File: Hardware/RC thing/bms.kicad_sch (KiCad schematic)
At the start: 6 parts, among them U1 MCP73831-2-OT

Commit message: 90%
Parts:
- added C401: 10u, Capacitor_SMD:C_0805_2012Metric_Pad1.18x1.45mm_HandSolder, symbol Device:C
- added C404: 22u, Capacitor_SMD:C_0805_2012Metric_Pad1.18x1.45mm_HandSolder, symbol Device:C
- added L402: 2.2u, Inductor_SMD:L_APV_ANR252012, symbol Device:L
- added R403: 100k, Resistor_SMD:R_0603_1608Metric_Pad0.98x0.95mm_HandSolder, symbol Device:R
- added R404: 160k, Resistor_SMD:R_0603_1608Metric_Pad0.98x0.95mm_HandSolder, symbol Device:R
- added R405: 51k, Resistor_SMD:R_0603_1608Metric_Pad0.98x0.95mm_HandSolder, symbol Device:R
- added U401: TPS62170DSG, Package_SON:WSON-8-1EP_2x2mm_P0.5mm_EP0.9x1.6mm_ThermalVias, symbol Regulator_Switching:TPS62170DSG
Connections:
- net +3.3V: now also C404.1, L402.2, R403.2, R404.2, U401.6 (VOS)
- net GND: now also C401.2, C404.2, R403.1, R405.1, U401.1 (PGND), U401.4 (AGND), U401.8 (PG), U401.9 (PAD)
- net VBAT: now also C401.1, U401.2 (VIN), U401.3 (EN)
- net VDC renamed VUSB
- new net: R404.1, R405.2, U401.5 (FB)
- new net: L402.1, U401.7 (SW)
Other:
- note added: "Buck converter - 3.3V"

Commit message: more rc stuff (trust)
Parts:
- removed R1: R, symbol Device:R
- added C409: 100n, Capacitor_SMD:C_0603_1608Metric_Pad1.08x0.95mm_HandSolder, symbol Device:C
- added R410: 200k, Resistor_SMD:R_0603_1608Metric_Pad0.98x0.95mm_HandSolder, symbol Device:R
- added R411: 130k, Resistor_SMD:R_0603_1608Metric_Pad0.98x0.95mm_HandSolder, symbol Device:R
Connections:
- net GND: now also C409.2, R411.2
- net VBAT: now also R410.1
- net Batt_status renamed Charge_status
- new net Battery_voltage_level: C409.1, R410.2, R411.1
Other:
- note added: "BMS/Charging IC"
- note added: "Battery voltage level"
- moved on the sheet: BT1, C1, C2, C401, C404, L402, R2, R403, R404, R405, U1, U401

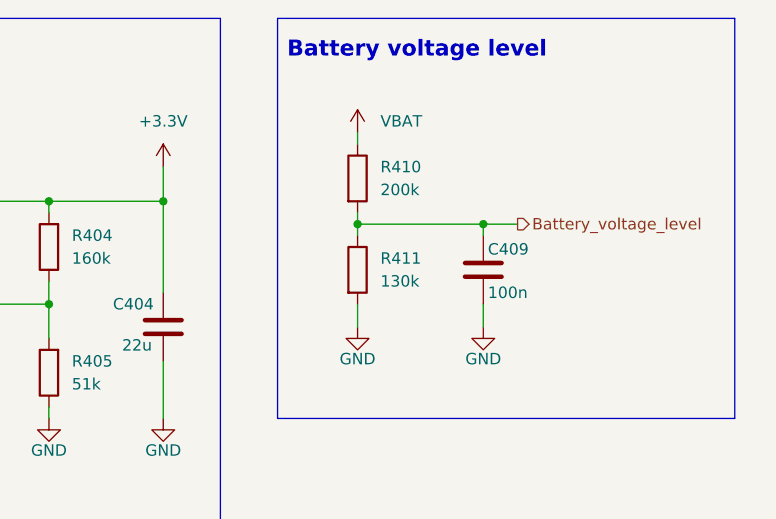
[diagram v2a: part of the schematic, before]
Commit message: fixed voltage divider for controller batt status
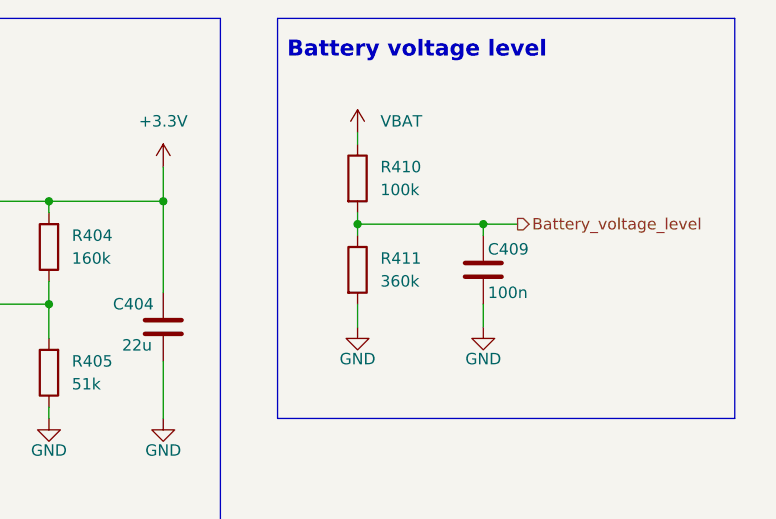
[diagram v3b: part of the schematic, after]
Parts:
- R410: value 200k -> 100k
- R411: value 130k -> 360k
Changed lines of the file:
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@@
 			)
 		)
-		(property "Value" "130k"
+		(property "Value" "360k"
 			(at 227.33 48.2599 0)
 			(effects
@@
 			)
 		)
-		(property "Value" "200k"
+		(property "Value" "100k"
 			(at 227.33 38.0999 0)
 			(effects

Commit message: RC thing PCB 95% trustworthy (six seven)
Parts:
- added D2: LED, Diode_SMD:D_0603_1608Metric_Pad1.05x0.95mm_HandSolder, symbol Device:LED
- added R1: 240, Resistor_SMD:R_0603_1608Metric_Pad0.98x0.95mm_HandSolder, symbol Device:R
- added SW1: Bat_switch, Connector_JST:JST_PH_B2B-PH-K_1x02_P2.00mm_Vertical, symbol Switch:SW_SPST
- BT1: footprint (none) -> Connector_JST:JST_PH_B2B-PH-K_1x02_P2.00mm_Vertical
- C18: renamed from C2; footprint (none) -> Capacitor_SMD:C_0805_2012Metric_Pad1.18x1.45mm_HandSolder
- C20: renamed from C1; footprint (none) -> Capacitor_SMD:C_0805_2012Metric_Pad1.18x1.45mm_HandSolder
- R2: footprint (none) -> Resistor_SMD:R_0603_1608Metric_Pad0.98x0.95mm_HandSolder
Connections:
- net Charge_status: now also D2.1 (K)
- net VBAT: now also SW1.2 (B); no longer BT1.1 (+)
- net +3.3V renamed +3V3
- net +3V3: now also R1.1
- new net: BT1.1 (+), SW1.1 (A)
- new net D2_in: D2.2 (A), R1.2
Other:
- moved on the sheet: BT1, C409, R410, R411

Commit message: new RC PCB updates
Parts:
- renumbered C401 to C31, C404 to C32, C409 to C33, L402 to L2, R403 to R35, R405 to R36, R404 to R37, R411 to R38, R410 to R39
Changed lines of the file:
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@@
 		(dnp no)
 		(fields_autoplaced yes)
-		(property "Reference" "R411"
+		(property "Reference" "R38"
 			(at 231.14 46.9899 0)
 			(effects
@@
 			(project "RC thing"
 				(path "/5c54a15d-2138-46dc-867e-29c9270be5e0/87ff3aa1-14e4-4935-92da-05f81d408638"
-					(reference "R411")
+					(reference "R38")
 					(unit 1)
 				)
@@
 		(dnp no)
 		(fields_autoplaced yes)
-		(property "Reference" "R403"
+		(property "Reference" "R35"
 			(at 179.07 57.1499 0)
 			(effects
@@
 			(project "RC thing"
 				(path "/5c54a15d-2138-46dc-867e-29c9270be5e0/87ff3aa1-14e4-4935-92da-05f81d408638"
-					(reference "R403")
+					(reference "R35")
 					(unit 1)
 				)
@@
 		(dnp no)
 		(fields_autoplaced yes)
-		(property "Reference" "L402"
+		(property "Reference" "L2"
 			(at 170.18 34.29 90)
 			(effects
@@
 			(project "RC thing"
 				(path "/5c54a15d-2138-46dc-867e-29c9270be5e0/87ff3aa1-14e4-4935-92da-05f81d408638"
-					(reference "L402")
+					(reference "L2")
 					(unit 1)
 				)
@@
 		(on_board yes)
 		(dnp no)
-		(property "Reference" "C409"
+		(property "Reference" "C33"
 			(at 243.078 45.974 0)
 			(effects
@@
 			(project "RC thing"
 				(path "/5c54a15d-2138-46dc-867e-29c9270be5e0/87ff3aa1-14e4-4935-92da-05f81d408638"
-					(reference "C409")
+					(reference "C33")
 					(unit 1)
 				)
@@
 		(dnp no)
 		(fields_autoplaced yes)
-		(property "Reference" "R410"
+		(property "Reference" "R39"
 			(at 231.14 36.8299 0)
 			(effects
@@
 			(project "RC thing"
 				(path "/5c54a15d-2138-46dc-867e-29c9270be5e0/87ff3aa1-14e4-4935-92da-05f81d408638"
-					(reference "R410")
+					(reference "R39")
 					(unit 1)
 				)
@@
 		(dnp no)
 		(fields_autoplaced yes)
-		(property "Reference" "R404"
+		(property "Reference" "R37"
 			(at 193.04 43.1799 0)
 			(effects
@@
 			(project "RC thing"
 				(path "/5c54a15d-2138-46dc-867e-29c9270be5e0/87ff3aa1-14e4-4935-92da-05f81d408638"
-					(reference "R404")
+					(reference "R37")
 					(unit 1)
 				)
@@
 		(on_board yes)
 		(dnp no)
-		(property "Reference" "C404"
+		(property "Reference" "C32"
 			(at 197.612 50.8 0)
 			(effects
@@
 			(project "RC thing"
 				(path "/5c54a15d-2138-46dc-867e-29c9270be5e0/87ff3aa1-14e4-4935-92da-05f81d408638"
-					(reference "C404")
+					(reference "C32")
 					(unit 1)
 				)
@@
 		(dnp no)
 		(fields_autoplaced yes)
-		(property "Reference" "R405"
+		(property "Reference" "R36"
 			(at 193.04 57.1499 0)
 			(effects
@@
 			(project "RC thing"
 				(path "/5c54a15d-2138-46dc-867e-29c9270be5e0/87ff3aa1-14e4-4935-92da-05f81d408638"
-					(reference "R405")
+					(reference "R36")
 					(unit 1)
 				)
@@
 		(on_board yes)
 		(dnp no)
-		(property "Reference" "C401"
+		(property "Reference" "C31"
 			(at 129.286 45.72 0)
 			(effects
@@
 			(project "RC thing"
 				(path "/5c54a15d-2138-46dc-867e-29c9270be5e0/87ff3aa1-14e4-4935-92da-05f81d408638"
-					(reference "C401")
-					(unit 1)
-				)
+					(reference "C31")
+					(unit 1)
+				)

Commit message: Reviewed .sch
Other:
- moved on the sheet: C18, C20
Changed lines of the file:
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@@
 	)
 	(junction
-		(at 76.2 40.64)
+		(at 50.8 60.96)
+		(diameter 0)
+		(color 0 0 0 0)
+	)
+	(junction
+		(at 77.47 40.64)
 		(diameter 0)
 		(color 0 0 0 0)
@@
 	(wire
 		(pts
+			(xy 50.8 60.96) (xy 50.8 63.5)
+		)
+		(stroke
+			(width 0)
+			(type default)
+		)
+	)
+	(wire
+		(pts
 			(xy 176.53 41.91) (xy 176.53 54.61)
 		)
@@
 	(wire
 		(pts
+			(xy 49.53 63.5) (xy 50.8 63.5)
+		)
+		(stroke
+			(width 0)
+			(type default)
+		)
+	)
+	(wire
+		(pts
 			(xy 26.67 45.72) (xy 29.21 45.72)
 		)
@@
 	(wire
 		(pts
-			(xy 49.53 40.64) (xy 76.2 40.64)
+			(xy 49.53 40.64) (xy 77.47 40.64)
 		)
 		(stroke
@@
 	(wire
 		(pts
+			(xy 49.53 29.21) (xy 49.53 27.94)
+		)
+		(stroke
+			(width 0)
+			(type default)
+		)
+	)
+	(wire
+		(pts
 			(xy 29.21 57.15) (xy 26.67 57.15)
 		)
@@
 	(wire
 		(pts
-			(xy 76.2 40.64) (xy 96.52 40.64)
-		)
-		(stroke
-			(width 0)
-			(type default)
-		)
-	)
-	(wire
-		(pts
 			(xy 228.6 52.07) (xy 228.6 54.61)
 		)
@@
 	(wire
 		(pts
+			(xy 40.64 27.94) (xy 39.37 27.94)
+		)
+		(stroke
+			(width 0)
+			(type default)
+		)
+	)
+	(wire
+		(pts
 			(xy 22.86 27.94) (xy 39.37 27.94)
 		)
@@
 	(wire
 		(pts
+			(xy 77.47 40.64) (xy 96.52 40.64)
+		)
+		(stroke
+			(width 0)
+			(type default)
+		)
+	)
+	(wire
+		(pts
 			(xy 143.51 41.91) (xy 133.35 41.91)
 		)
@@
 	(wire
 		(pts
+			(xy 77.47 41.91) (xy 77.47 40.64)
+		)
+		(stroke
+			(width 0)
+			(type default)
+		)
+	)
+	(wire
+		(pts
 			(xy 203.2 35.56) (xy 203.2 39.37)
 		)
@@
 	(wire
 		(pts
+			(xy 77.47 50.8) (xy 77.47 49.53)
+		)
+		(stroke
+			(width 0)
+			(type default)
+		)
+	)
+	(wire
+		(pts
 			(xy 176.53 63.5) (xy 176.53 62.23)
 		)
@@
 	(wire
 		(pts
-			(xy 46.99 27.94) (xy 49.53 27.94)
-		)
-		(stroke
-			(width 0)
-			(type default)
-		)
-	)
-	(wire
-		(pts
 			(xy 22.86 27.94) (xy 22.86 26.67)
 		)
@@
 		(pts
 			(xy 228.6 43.18) (xy 228.6 44.45)
+		)
+		(stroke
+			(width 0)
+			(type default)
+		)
+	)
+	(wire
+		(pts
+			(xy 49.53 27.94) (xy 48.26 27.94)
 		)
 		(stroke
@@
 	(hierarchical_label "Charge_status"
 		(shape output)
-		(at 50.8 45.72 0)
+		(at 49.53 63.5 180)
 		(effects
 			(font
 				(size 1.27 1.27)
 			)
-			(justify left)
+			(justify right)
 		)
 	)
@@
 	(symbol
 		(lib_id "Device:C_Polarized")
-		(at 43.18 27.94 90)
+		(at 44.45 27.94 90)
 		(unit 1)
 		(exclude_from_sim no)
@@
 		(fields_autoplaced yes)
 		(property "Reference" "C20"
-			(at 42.291 20.32 90)
+			(at 43.561 20.32 90)
 			(effects
 				(font
@@
 		)
 		(property "Value" "4.7u"
-			(at 42.291 22.86 90)
+			(at 43.561 22.86 90)
 			(effects
 				(font
@@
 		)
 		(property "Footprint" "Capacitor_SMD:C_0805_2012Metric_Pad1.18x1.45mm_HandSolder"
-			(at 46.99 26.9748 0)
+			(at 48.26 26.9748 0)
 			(effects
 				(font
@@
 		)
 		(property "Datasheet" "~"
-			(at 43.18 27.94 0)
+			(at 44.45 27.94 0)
 			(effects
 				(font
@@
 		)
 		(property "Description" "Polarized capacitor"
-			(at 43.18 27.94 0)
+			(at 44.45 27.94 0)
 			(effects
 				(font
@@
 	(symbol
 		(lib_id "Device:C_Polarized")
-		(at 76.2 44.45 0)
+		(at 77.47 45.72 0)
 		(unit 1)
 		(exclude_from_sim no)
@@
 		(dnp no)
 		(property "Reference" "C18"
-			(at 80.01 42.2909 0)
+			(at 81.28 43.5609 0)
 			(effects
 				(font
@@
 		)
 		(property "Value" "4.7u"
-			(at 80.01 44.8309 0)
+			(at 81.28 46.1009 0)
 			(effects
 				(font
@@
 		)
 		(property "Footprint" "Capacitor_SMD:C_0805_2012Metric_Pad1.18x1.45mm_HandSolder"
-			(at 77.1652 48.26 0)
+			(at 78.4352 49.53 0)
 			(effects
 				(font
@@
 		)
 		(property "Datasheet" "~"
-			(at 76.2 44.45 0)
+			(at 77.47 45.72 0)
 			(effects
 				(font
@@
 		)
 		(property "Description" "Polarized capacitor"
-			(at 76.2 44.45 0)
+			(at 77.47 45.72 0)
 			(effects
 				(font
@@
 		(on_board yes)
 		(dnp no)
-		(fields_autoplaced yes)
 		(property "Reference" "#PWR01"
 			(at 67.31 50.8 0)
@@
 		)
 		(property "Value" "+3V3"
-			(at 67.31 41.91 0)
+			(at 67.31 43.434 0)
 			(effects
 				(font
@@
 		(on_board yes)
 		(dnp no)
-		(fields_autoplaced yes)
 		(property "Reference" "#PWR05"
 			(at 39.37 63.5 0)
@@
 		)
 		(property "Value" "GND"
-			(at 39.37 62.23 0)
+			(at 39.37 60.706 0)
 			(effects
 				(font
@@
 		(on_board yes)
 		(dnp no)
-		(fields_autoplaced yes)
 		(property "Reference" "#PWR0411"
 			(at 176.53 69.85 0)
@@
 		)
 		(property "Value" "GND"
-			(at 176.53 68.58 0)
+			(at 176.53 67.31 0)
 			(effects
 				(font
@@
 	(symbol
 		(lib_id "power:GND")
-		(at 49.53 27.94 0)
-		(unit 1)
-		(exclude_from_sim no)
-		(in_bom yes)
-		(on_board yes)
-		(dnp no)
-		(fields_autoplaced yes)
+		(at 49.53 29.21 0)
+		(unit 1)
+		(exclude_from_sim no)
+		(in_bom yes)
+		(on_board yes)
+		(dnp no)
 		(property "Reference" "#PWR02"
-			(at 49.53 34.29 0)
+			(at 49.53 35.56 0)
 			(effects
 				(font
@@
 		)
 		(property "Value" "GND"
-			(at 49.53 33.02 0)
+			(at 49.53 32.766 0)
 			(effects
 				(font
@@
 		)
 		(property "Footprint" ""
-			(at 49.53 27.94 0)
+			(at 49.53 29.21 0)
 			(effects
 				(font
@@
 		)
 		(property "Datasheet" ""
-			(at 49.53 27.94 0)
+			(at 49.53 29.21 0)
 			(effects
 				(font
@@
 		)
 		(property "Description" "Power symbol creates a global label with name \"GND\" , ground"
-			(at 49.53 27.94 0)
+			(at 49.53 29.21 0)
 			(effects
 				(font
@@
 	(symbol
 		(lib_id "power:GND")
-		(at 76.2 48.26 0)
+		(at 77.47 50.8 0)
 		(unit 1)
 		(exclude_from_sim no)
@@
 		(fields_autoplaced yes)
 		(property "Reference" "#PWR03"
-			(at 76.2 54.61 0)
+			(at 77.47 57.15 0)
 			(effects
 				(font
@@
 		)
 		(property "Value" "GND"
-			(at 76.2 53.34 0)
+			(at 77.47 55.88 0)
 			(effects
 				(font
@@
 		)
 		(property "Footprint" ""
-			(at 76.2 48.26 0)
+			(at 77.47 50.8 0)
 			(effects
 				(font
@@
 		)
 		(property "Datasheet" ""
-			(at 76.2 48.26 0)
+			(at 77.47 50.8 0)
 			(effects
 				(font
@@
 		)
 		(property "Description" "Power symbol creates a global label with name \"GND\" , ground"
-			(at 76.2 48.26 0)
+			(at 77.47 50.8 0)
 			(effects
 				(font
@@
 		(on_board yes)
 		(dnp no)
-		(fields_autoplaced yes)
 		(property "Reference" "U1"
-			(at 41.5133 33.02 0)
+			(at 40.64 34.29 0)
 			(effects
 				(font
@@
 		)
 		(property "Value" "MCP73831-2-OT"
-			(at 41.5133 35.56 0)
-			(effects
-				(font
+			(at 40.64 36.83 0)
+			(effects
+				(font

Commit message: Final touches
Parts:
- renumbered C20 to C15, C18 to C16, C31 to C17, C32 to C18, C33 to C19, L2 to L1, R2 to R11, R1 to R12, R35 to R13, R37 to R14, R36 to R15, R39 to R16, R38 to R17, SW1 to SW6, U1 to U4, U401 to U5
